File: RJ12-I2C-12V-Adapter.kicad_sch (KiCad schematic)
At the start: 8 parts, among them J1 6P6C, J10 I²C, J11 Relais-Power, J2 6P6C

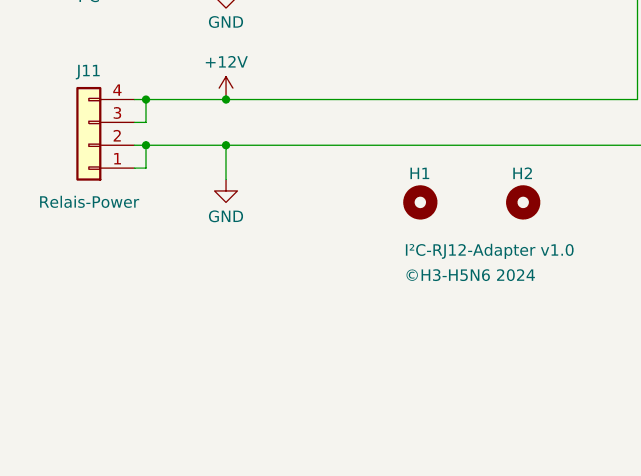
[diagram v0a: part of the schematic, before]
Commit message: Extra Anschlüsse für 12V/GND, RJ12 ganz an den Rand geschoben
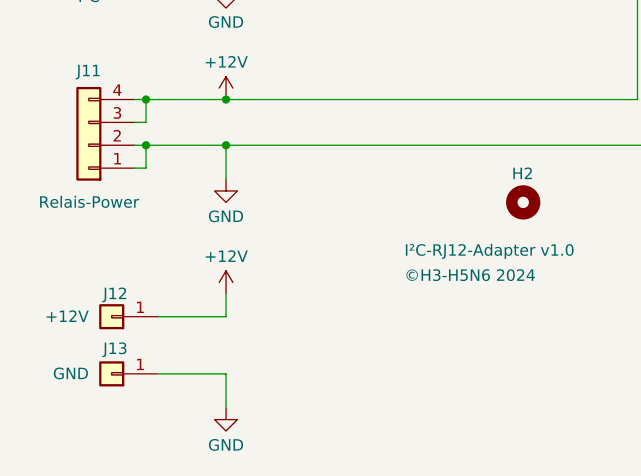
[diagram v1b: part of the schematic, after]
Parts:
- removed H1: MountingHole, MountingHole:MountingHole_3.2mm_M3, symbol Mechanical:MountingHole
- added J12: +12V, Wago:Pad_7.5x2.2mm, symbol Connector_Generic:Conn_01x01
- added J13: GND, Wago:Pad_7.5x2.2mm, symbol Connector_Generic:Conn_01x01
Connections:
- net +12V: now also J12.1 (Pin_1)
- net GND: now also J13.1 (Pin_1)
